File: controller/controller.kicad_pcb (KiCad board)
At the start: 2 copper layers, 50 x 23 mm, 32 parts, among them J1 ICSP, J2 USB_B_Micro, J3 TRRS_Jack, J4 6P_ZH_connector, J5 6P_ZH_connector, SW1 RESET, U3 ATmega32U4-AU, Y1 16MHz

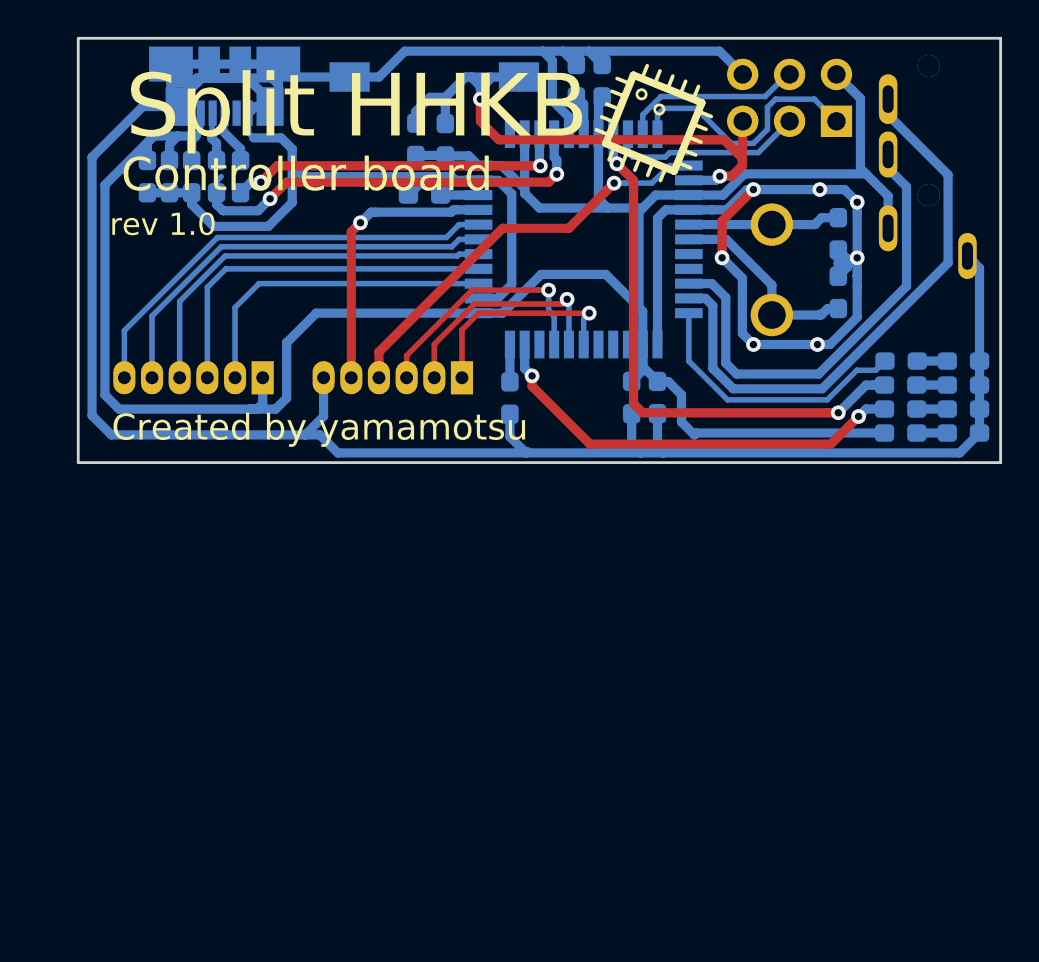
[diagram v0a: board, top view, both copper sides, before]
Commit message: [add] controller rev2.0
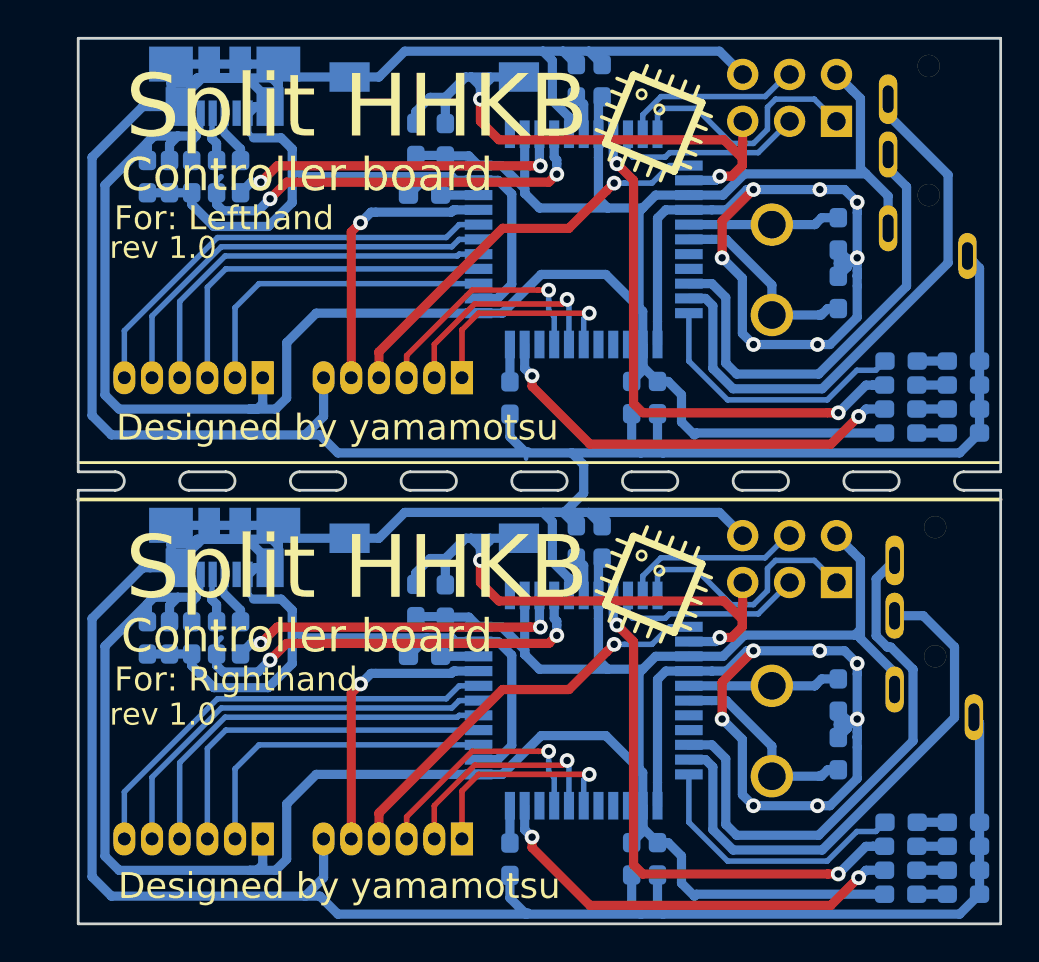
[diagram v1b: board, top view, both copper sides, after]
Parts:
- added C10: 100n, Capacitor_SMD:C_0603_1608Metric_Pad1.05x0.95mm_HandSolder, B.Cu at (68.8, 83.5)
- added C11: 0.1u, Capacitor_SMD:C_0603_1608Metric_Pad1.05x0.95mm_HandSolder, B.Cu at (78.4, 77.3)
- added C12: 1u, Capacitor_SMD:C_0603_1608Metric_Pad1.05x0.95mm_HandSolder, B.Cu at (77.0, 77.3)
- added C13: 1u, Capacitor_SMD:C_0603_1608Metric_Pad1.05x0.95mm_HandSolder, B.Cu at (81.4, 94.5)
- added C14: 1u, Capacitor_SMD:C_0603_1608Metric_Pad1.05x0.95mm_HandSolder, B.Cu at (80.0, 94.5)
- added C15: 0.1u, Capacitor_SMD:C_0603_1608Metric_Pad1.05x0.95mm_HandSolder, B.Cu at (55.0, 82.5)
- added C16: 22u, Capacitor_SMD:C_0603_1608Metric_Pad1.05x0.95mm_HandSolder, B.Cu at (53.8, 82.5)
- added C8: 22p, Capacitor_SMD:C_0603_1608Metric_Pad1.05x0.95mm_HandSolder, B.Cu at (91.2, 88.8)
- added C9: 22p, Capacitor_SMD:C_0603_1608Metric_Pad1.05x0.95mm_HandSolder, B.Cu at (91.2, 85.6)
- added D1: D, Diode_SMD:D_0603_1608Metric_Pad1.05x0.95mm_HandSolder, B.Cu at (69.9, 80.5)
- added D2: L, Diode_SMD:D_0603_1608Metric_Pad1.05x0.95mm_HandSolder, B.Cu at (98.0, 95.1)
- added D3: RX, Diode_SMD:D_0603_1608Metric_Pad1.05x0.95mm_HandSolder, B.Cu at (98.0, 93.8)
- added D4: TX, Diode_SMD:D_0603_1608Metric_Pad1.05x0.95mm_HandSolder, B.Cu at (98.0, 92.5)
- added D5: PWR, Diode_SMD:D_0603_1608Metric_Pad1.05x0.95mm_HandSolder, B.Cu at (98.0, 96.4)
- added J1: ICSP, Connector_PinHeader_2.54mm:PinHeader_2x03_P2.54mm_Vertical, B.Cu at (91.1, 79.5)
- added J2: USB_B_Micro, Connector_USB:USB_Micro-B_Molex_47346-0001, B.Cu at (57.9, 77.6)
- added J3: TRRS_Jack, MyLib:TRRS_jack_MJ4PP9, B.Cu at (96.5, 75.0)
- added J4: 6P_ZH_connector, MyLib:ZH_6P_Horizontal, B.Cu at (60.0, 93.4)
- added J5: 6P_ZH_connector, MyLib:ZH_6P_Horizontal, B.Cu at (70.8, 93.4)
- added R16: 10k, Resistor_SMD:R_0603_1608Metric_Pad1.05x0.95mm_HandSolder, B.Cu at (68.3, 80.5)
- added R17: 1k, Resistor_SMD:R_0603_1608Metric_Pad1.05x0.95mm_HandSolder, B.Cu at (94.6, 95.1)
- added R18: 1k, Resistor_SMD:R_0603_1608Metric_Pad1.05x0.95mm_HandSolder, B.Cu at (94.6, 93.8)
- added R19: 1k, Resistor_SMD:R_0603_1608Metric_Pad1.05x0.95mm_HandSolder, B.Cu at (94.6, 92.5)
- added R20: 1k, Resistor_SMD:R_0603_1608Metric_Pad1.05x0.95mm_HandSolder, B.Cu at (94.6, 96.4)
- added R21: 10k, Resistor_SMD:R_0603_1608Metric_Pad1.05x0.95mm_HandSolder, B.Cu at (73.4, 94.5)
- added R22: 22, Resistor_SMD:R_0603_1608Metric_Pad1.05x0.95mm_HandSolder, B.Cu at (58.8, 82.5)
- added R23: 22, Resistor_SMD:R_0603_1608Metric_Pad1.05x0.95mm_HandSolder, B.Cu at (57.5, 82.5)
- added R24: 100k, Resistor_SMD:R_0603_1608Metric_Pad1.05x0.95mm_HandSolder, B.Cu at (56.1, 82.5)
- added REF**: IC_Sticker, MyLib:IC_Sticker, F.Cu at (81.2, 79.6)
- added SW1: RESET, Button_Switch_SMD:SW_SPST_FSMSM, B.Cu at (69.3, 77.1)
- added U3: ATmega32U4-AU, Package_QFP:TQFP-44_10x10mm_P0.8mm, B.Cu at (77.4, 85.9)
- added Y1: 16MHz, Crystal:Crystal_HC50_Vertical, B.Cu at (87.6, 90.0)
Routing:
- net GND: track 233.0 -> 470.8 mm, vias 7 -> 14
- net +5V: track 132.6 -> 265.1 mm
- net /RESET: track 33.4 -> 66.9 mm, vias 2 -> 4
- net /Rx: track 25.4 -> 55.0 mm
- net /RXLED: track 29.5 -> 59.0 mm, vias 2 -> 4
- net /Tx: track 31.1 -> 60.3 mm
- net /DRAIN: track 24.1 -> 48.3 mm
- net /CLKLED: track 23.6 -> 47.2 mm, vias 2 -> 4
- net /D-: track 23.2 -> 46.5 mm, vias 2 -> 4
- net /MUX_EN: track 22.8 -> 45.5 mm
- net /COL_EN: track 22.4 -> 44.8 mm, vias 1 -> 2
- net /MUX_C: track 21.4 -> 42.8 mm
- net /MUX_B: track 20.0 -> 40.0 mm
- net /D+: track 18.6 -> 37.2 mm, vias 2 -> 4
- net /MUX_A: track 17.5 -> 35.1 mm
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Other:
- board size 50 x 23 mm -> 50 x 48 mm
- board text added: "Designed by yamamotsu"
- board text added: "For: Lefthand"
- board text added: "For: Righthand"
- board text removed: "Created by yamamotsu"

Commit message: [add] step files
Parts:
- removed the C10 at (68.8, 83.5)
- removed the C11 at (78.4, 77.3)
- removed the C12 at (77.0, 77.3)
- removed the C13 at (81.4, 94.5)
- removed the C14 at (80.0, 94.5)
- removed the C15 at (55.0, 82.5)
- removed the C16 at (53.8, 82.5)
- removed the C8 at (91.2, 88.8)
- removed the C9 at (91.2, 85.6)
- removed the D1 at (69.9, 80.5)
- removed the D2 at (98.0, 95.1)
- removed the D3 at (98.0, 93.8)
- removed the D4 at (98.0, 92.5)
- removed the D5 at (98.0, 96.4)
- removed the J1 at (91.1, 79.5)
- removed the J2 at (57.9, 77.6)
- removed the J3 at (96.5, 75.0)
- removed the J4 at (60.0, 93.4)
- removed the J5 at (70.8, 93.4)
- removed the R16 at (68.3, 80.5)
- removed the R17 at (94.6, 95.1)
- removed the R18 at (94.6, 93.8)
- removed the R19 at (94.6, 92.5)
- removed the R20 at (94.6, 96.4)
- removed the R21 at (73.4, 94.5)
- removed the R22 at (58.8, 82.5)
- removed the R23 at (57.5, 82.5)
- removed the R24 at (56.1, 82.5)
- removed the REF** at (81.2, 79.6)
- removed the SW1 at (69.3, 77.1)
- removed the U3 at (77.4, 85.9)
- removed the Y1 at (87.6, 90.0)
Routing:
- net GND: track 470.8 -> 233.4 mm, vias 14 -> 7
- net +5V: track 265.1 -> 132.6 mm
- net /RESET: track 66.9 -> 33.4 mm, vias 4 -> 2
- net /Rx: track 55.0 -> 25.4 mm
- net /RXLED: track 59.0 -> 29.5 mm, vias 4 -> 2
- net /Tx: track 60.3 -> 31.1 mm
- net /DRAIN: track 48.3 -> 24.1 mm
- net /CLKLED: track 47.2 -> 23.6 mm, vias 4 -> 2
- net /D-: track 46.5 -> 23.2 mm, vias 4 -> 2
- net /MUX_EN: track 45.5 -> 22.8 mm
- net /COL_EN: track 44.8 -> 22.4 mm, vias 2 -> 1
- net /MUX_C: track 42.8 -> 21.4 mm
- net /MUX_B: track 40.0 -> 20.0 mm
- net /D+: track 37.2 -> 18.6 mm, vias 4 -> 2
- net /MUX_A: track 35.1 -> 17.5 mm
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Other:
- board size 50 x 48 mm -> 50 x 23 mm
- board text removed: "For: Righthand"
